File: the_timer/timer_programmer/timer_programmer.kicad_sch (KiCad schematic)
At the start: 7 parts, among them J1 AVR-ISP-6, J3 R41-B583A, U1 MCP2210x-SS

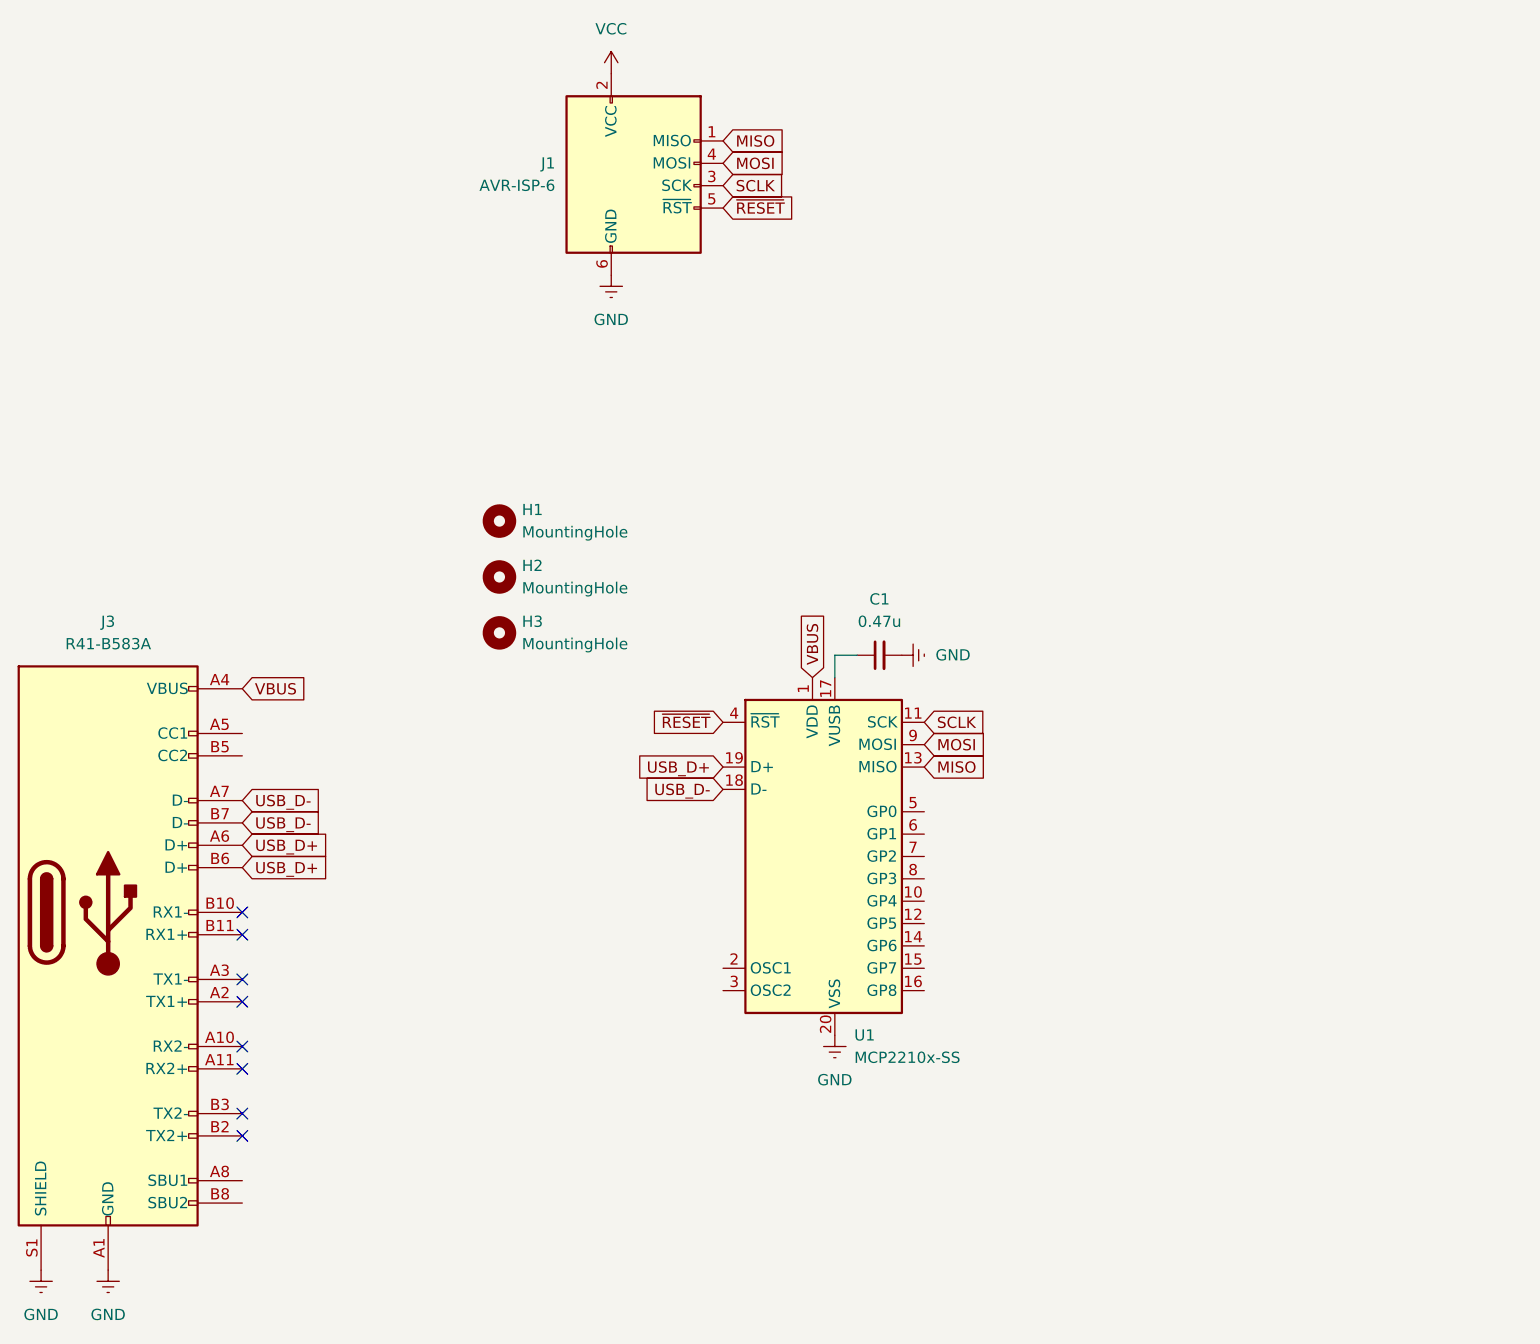
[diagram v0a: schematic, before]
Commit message: Finished routing Timer Programmer
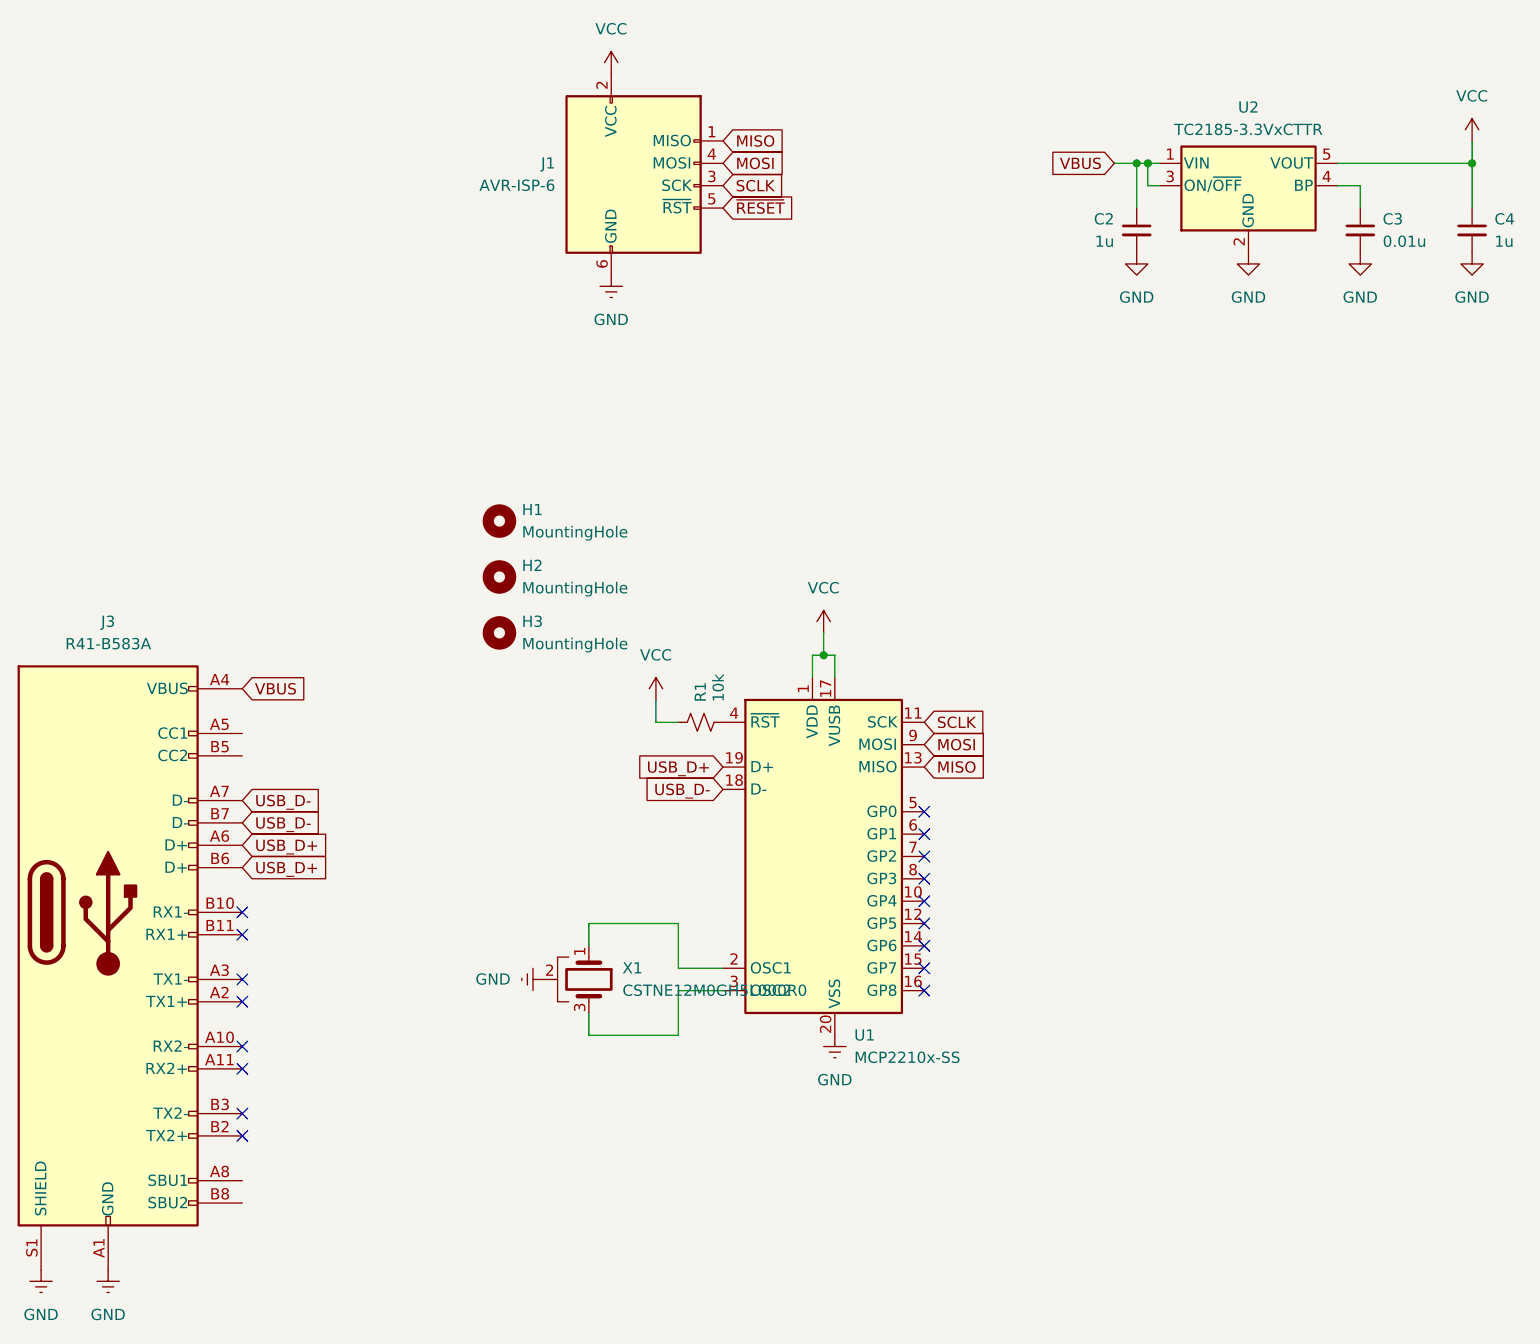
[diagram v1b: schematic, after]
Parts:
- removed C1: 0.47u, Capacitor_SMD:C_0603_1608Metric, symbol Device:C_Small
- added C2, C4: 1u, Capacitor_SMD:C_0603_1608Metric, symbol Device:C_Small
- added C3: 0.01u, Capacitor_SMD:C_0603_1608Metric, symbol Device:C_Small
- added R1: 10k, Resistor_SMD:R_0603_1608Metric, symbol Device:R_Small_US
- added U2: TC2185-3.3VxCTTR, Package_TO_SOT_SMD:SOT-23-5, symbol Regulator_Linear:TC2185-3.3VxCTTR
- added X1: CSTNE12M0GH5L000R0, Crystal:Resonator_SMD_Murata_CSTxExxV-3Pin_3.0x1.1mm, symbol Device:Crystal_GND2
- U1: DKPN (none) -> MCP2210T-I/SSCT-ND
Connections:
- net GND: now also C2.2, C3.2, C4.2, U2.2 (GND), X1.2
- net VBUS: now also C2.1, U2.1 (VIN), U2.3 (ON/~{OFF}); no longer U1.1 (VDD)
- net VCC: now also U1.1 (VDD), U1.17 (VUSB), C4.1, R1.1, U2.5 (VOUT)
- net ~{RESET}: no longer U1.4 (~{RST})
- net at U1.2 (OSC1): now also X1.1
- net at U1.3 (OSC2): now also X1.3
- new net: C3.1, U2.4 (BP)
- new net: R1.2, U1.4 (~{RST})
- no-connect marks 8 -> 17

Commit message: Redesigned Timer Programmer
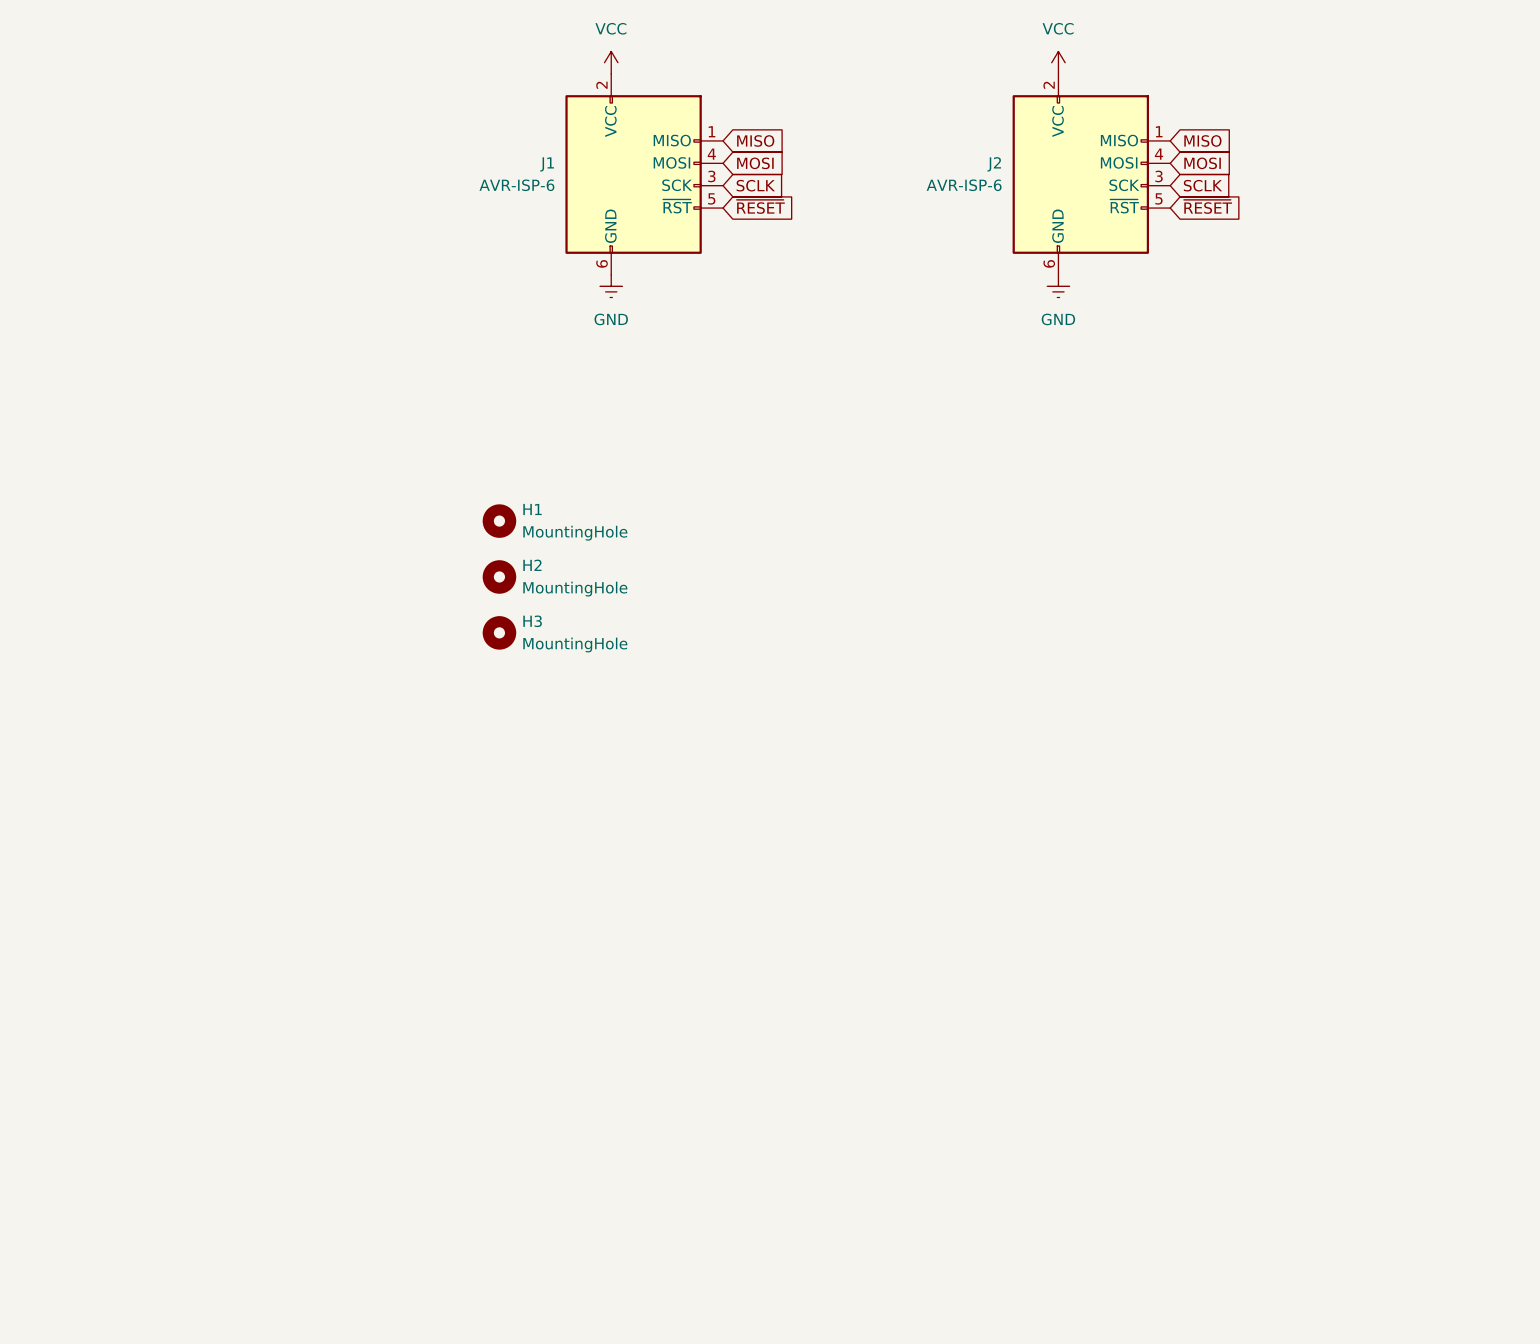
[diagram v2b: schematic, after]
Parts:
- removed C2, C4: 1u, Capacitor_SMD:C_0603_1608Metric, symbol Device:C_Small
- removed C3: 0.01u, Capacitor_SMD:C_0603_1608Metric, symbol Device:C_Small
- removed J3: R41-B583A, locals_but_working_PLEASE:CONN_R41-B583A_MIT, symbol Connector:USB_C_Receptacle
- removed R1: 10k, Resistor_SMD:R_0603_1608Metric, symbol Device:R_Small_US
- removed U1: MCP2210x-SS, Package_SO:SSOP-20_5.3x7.2mm_P0.65mm, symbol Interface_USB:MCP2210x-SS
- removed U2: TC2185-3.3VxCTTR, Package_TO_SOT_SMD:SOT-23-5, symbol Regulator_Linear:TC2185-3.3VxCTTR
- removed X1: CSTNE12M0GH5L000R0, Crystal:Resonator_SMD_Murata_CSTxExxV-3Pin_3.0x1.1mm, symbol Device:Crystal_GND2
- added J2: AVR-ISP-6, Connector_PinHeader_2.54mm:PinHeader_2x03_P2.54mm_Horizontal, symbol Connector:AVR-ISP-6
- J1: DKPN (none) -> 609-3752-ND
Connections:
- net GND: now also J2.6 (GND)
- net MISO: now also J2.1 (MISO)
- net MOSI: now also J2.4 (MOSI)
- net SCLK: now also J2.3 (SCK)
- net VCC: now also J2.2 (VCC)
- net ~{RESET}: now also J2.5 (~{RST})
- no-connect marks 17 -> 0
